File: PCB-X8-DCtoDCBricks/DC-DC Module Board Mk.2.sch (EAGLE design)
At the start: 151 parts, among them T1 FDN340P, T2 AP1117_LIN_REG, U3 LM1085IS-5.0

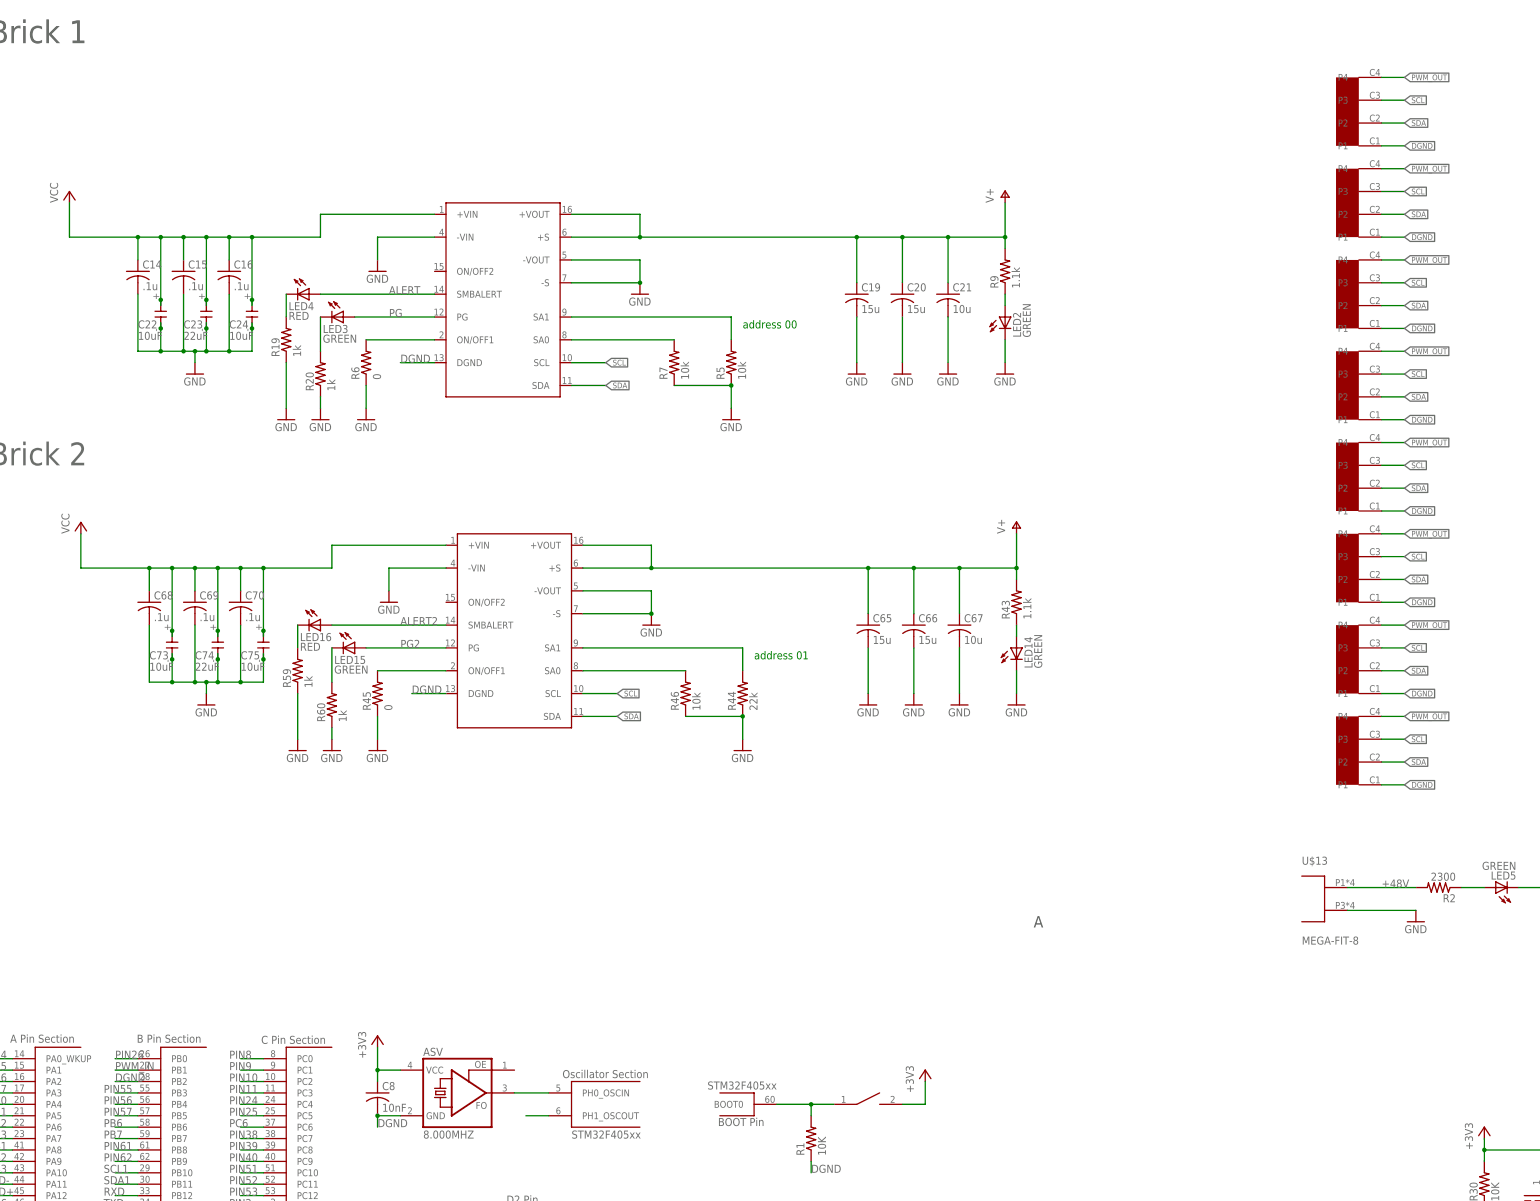
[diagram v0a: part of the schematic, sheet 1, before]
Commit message: top GND plane and clean up
Added top ground plane, cleaned up messy signals and other mistakes
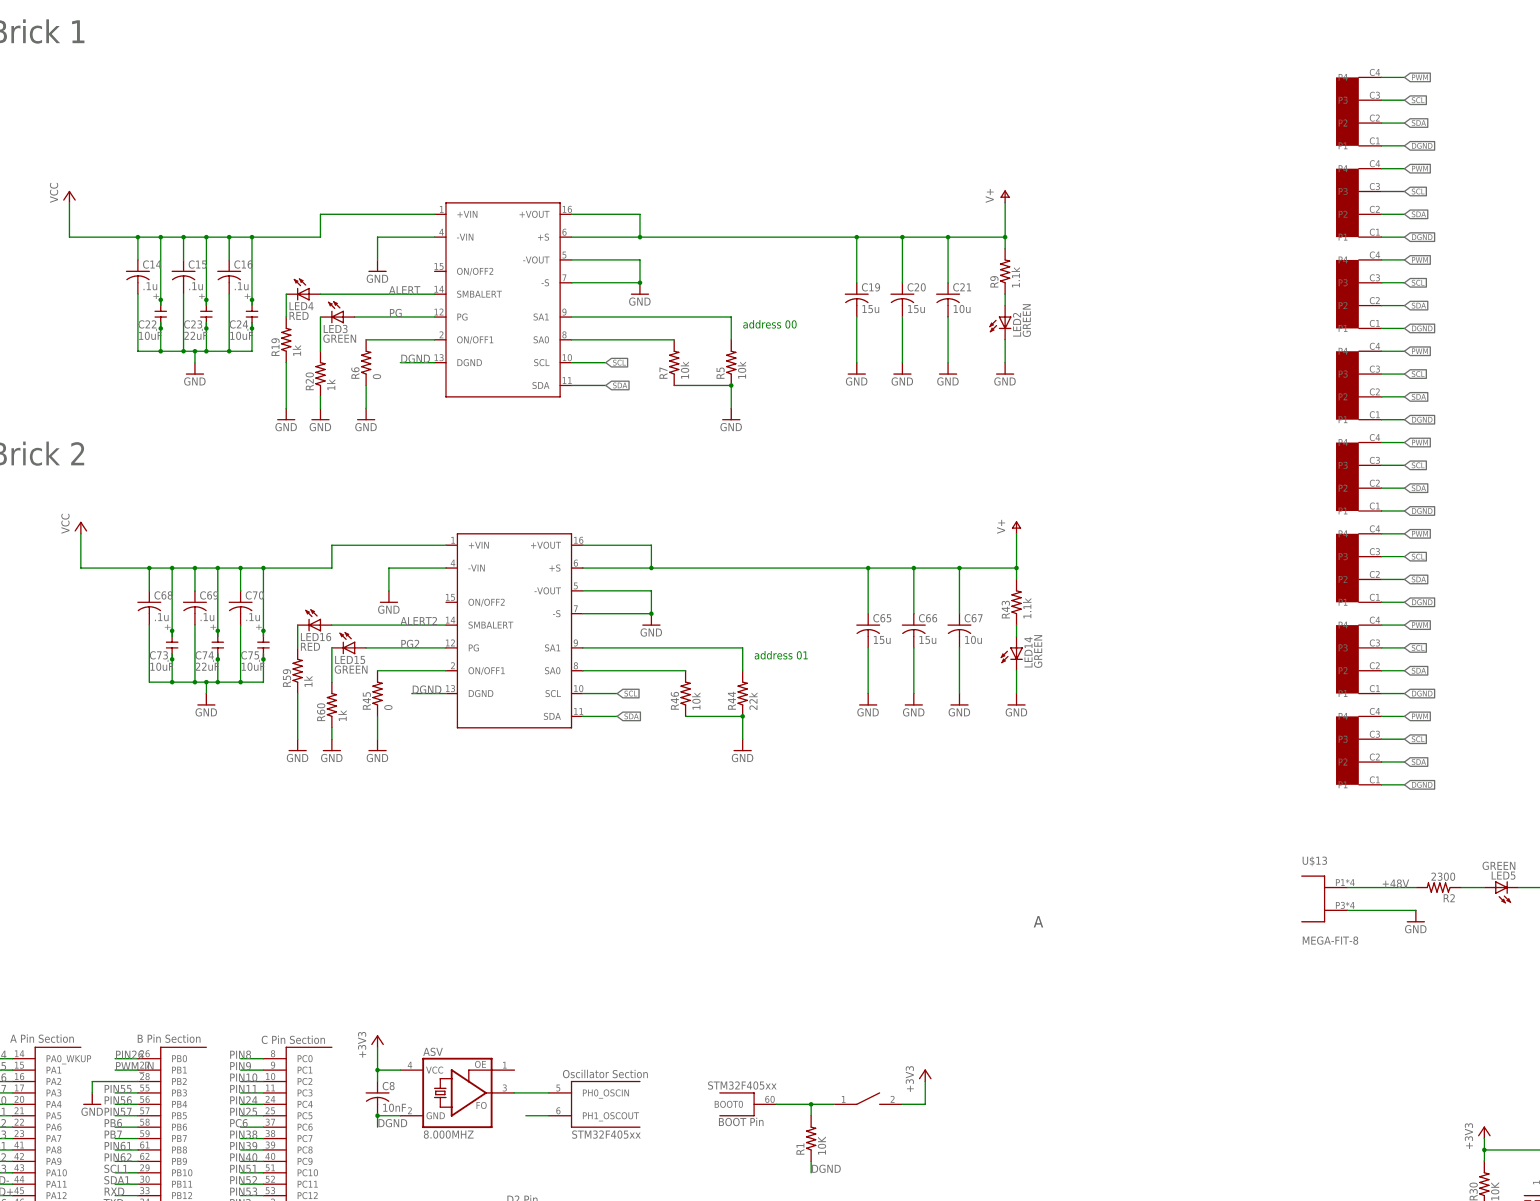
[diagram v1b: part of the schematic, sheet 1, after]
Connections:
- new net PWM: U$15.P4, U$20.P4, U$23.P4, U$24.P4, U$25.P4, U$26.P4, U$27.P4, U$28.P4
- net DGND: no longer U$5G$2.PB2
- net GND: now also U$5G$2.PB2
- net PWM_OUT: no longer U$15.P4, U$20.P4, U$23.P4, U$24.P4, U$25.P4, U$26.P4, U$27.P4, U$28.P4
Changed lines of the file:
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@@
 <?xml version="1.0" encoding="utf-8"?>
 <!DOCTYPE eagle SYSTEM "eagle.dtd">
-<eagle version="7.4.0">
+<eagle version="7.2.0">
 <drawing>
 <settings>
@@
 <part name="+3V3" library="supply1" deviceset="+3V3" device=""/>
 <part name="+3V4" library="supply1" deviceset="+3V3" device=""/>
+<part name="GND21" library="supply1" deviceset="GND" device=""/>
 <part name="FRAME3" library="frames" deviceset="FRAME_A_L" device=""/>
 <part name="D3" library="SparkFun-LED" deviceset="LED-YELLOW" device="0603" value="Yellow"/>
@@
 <instance part="+3V3" gate="G$1" x="193.04" y="-63.5"/>
 <instance part="+3V4" gate="G$1" x="99.06" y="-12.7"/>
+<instance part="GND21" gate="1" x="35.56" y="-27.94"/>
 <instance part="FRAME3" gate="G$1" x="292.1" y="-220.98"/>
 <instance part="FRAME3" gate="G$2" x="462.28" y="-220.98"/>
@@
 <wire x1="111.76" y1="165.1" x2="99.06" y2="165.1" width="0.1524" layer="91"/>
 <wire x1="99.06" y1="165.1" x2="99.06" y2="160.02" width="0.1524" layer="91"/>
+</segment>
+<segment>
+<pinref part="U$5" gate="G$2" pin="PB2"/>
+<wire x1="45.72" y1="-22.86" x2="35.56" y2="-22.86" width="0.1524" layer="91"/>
+<wire x1="35.56" y1="-22.86" x2="35.56" y2="-25.4" width="0.1524" layer="91"/>
+<pinref part="GND21" gate="1" pin="GND"/>
 </segment>
 <segment>
@@
 <label x="88.9" y="-213.36" size="1.778" layer="95"/>
 </segment>
-<segment>
-<pinref part="U$5" gate="G$2" pin="PB2"/>
-<wire x1="45.72" y1="-22.86" x2="40.64" y2="-22.86" width="0.1524" layer="91"/>
-<label x="40.64" y="-22.86" size="1.778" layer="95"/>
-</segment>
 </net>
 <net name="VCAP_1" class="0">
@@
 </segment>
 </net>
+<net name="PWM" class="0">
+<segment>
+<pinref part="U$15" gate="G$1" pin="P4"/>
+<wire x1="322.58" y1="200.66" x2="327.66" y2="200.66" width="0.1524" layer="91"/>
+<label x="327.66" y="200.66" size="1.27" layer="95" xref="yes"/>
+</segment>
+<segment>
+<pinref part="U$20" gate="G$1" pin="P4"/>
+<wire x1="322.58" y1="180.34" x2="327.66" y2="180.34" width="0.1524" layer="91"/>
+<label x="327.66" y="180.34" size="1.27" layer="95" xref="yes"/>
+</segment>
+<segment>
+<pinref part="U$23" gate="G$1" pin="P4"/>
+<wire x1="322.58" y1="160.02" x2="327.66" y2="160.02" width="0.1524" layer="91"/>
+<label x="327.66" y="160.02" size="1.27" layer="95" xref="yes"/>
+</segment>
+<segment>
+<pinref part="U$24" gate="G$1" pin="P4"/>
+<wire x1="322.58" y1="139.7" x2="327.66" y2="139.7" width="0.1524" layer="91"/>
+<label x="327.66" y="139.7" size="1.27" layer="95" xref="yes"/>
+</segment>
+<segment>
+<pinref part="U$25" gate="G$1" pin="P4"/>
+<wire x1="322.58" y1="119.38" x2="327.66" y2="119.38" width="0.1524" layer="91"/>
+<label x="327.66" y="119.38" size="1.27" layer="95" xref="yes"/>
+</segment>
+<segment>
+<pinref part="U$26" gate="G$1" pin="P4"/>
+<wire x1="322.58" y1="99.06" x2="327.66" y2="99.06" width="0.1524" layer="91"/>
+<label x="327.66" y="99.06" size="1.27" layer="95" xref="yes"/>
+</segment>
+<segment>
+<pinref part="U$27" gate="G$1" pin="P4"/>
+<wire x1="322.58" y1="78.74" x2="327.66" y2="78.74" width="0.1524" layer="91"/>
+<label x="327.66" y="78.74" size="1.27" layer="95" xref="yes"/>
+</segment>
+<segment>
+<pinref part="U$28" gate="G$1" pin="P4"/>
+<wire x1="322.58" y1="58.42" x2="327.66" y2="58.42" width="0.1524" layer="91"/>
+<label x="327.66" y="58.42" size="1.27" layer="95" xref="yes"/>
+</segment>
+</net>
 <net name="+12V4" class="0">
 <segment>
@@
 <label x="441.96" y="167.64" size="1.27" layer="95" xref="yes"/>
 </segment>
-<segment>
-<pinref part="U$28" gate="G$1" pin="P4"/>
-<wire x1="322.58" y1="58.42" x2="327.66" y2="58.42" width="0.1524" layer="91"/>
-<label x="327.66" y="58.42" size="1.27" layer="95" xref="yes"/>
-</segment>
-<segment>
-<pinref part="U$15" gate="G$1" pin="P4"/>
-<wire x1="322.58" y1="200.66" x2="327.66" y2="200.66" width="0.1524" layer="91"/>
-<label x="327.66" y="200.66" size="1.27" layer="95" xref="yes"/>
-</segment>
-<segment>
-<pinref part="U$20" gate="G$1" pin="P4"/>
-<wire x1="322.58" y1="180.34" x2="327.66" y2="180.34" width="0.1524" layer="91"/>
-<label x="327.66" y="180.34" size="1.27" layer="95" xref="yes"/>
-</segment>
-<segment>
-<pinref part="U$23" gate="G$1" pin="P4"/>
-<wire x1="322.58" y1="160.02" x2="327.66" y2="160.02" width="0.1524" layer="91"/>
-<label x="327.66" y="160.02" size="1.27" layer="95" xref="yes"/>
-</segment>
-<segment>
-<pinref part="U$24" gate="G$1" pin="P4"/>
-<wire x1="322.58" y1="139.7" x2="327.66" y2="139.7" width="0.1524" layer="91"/>
-<label x="327.66" y="139.7" size="1.27" layer="95" xref="yes"/>
-</segment>
-<segment>
-<pinref part="U$25" gate="G$1" pin="P4"/>
-<wire x1="322.58" y1="119.38" x2="327.66" y2="119.38" width="0.1524" layer="91"/>
-<label x="327.66" y="119.38" size="1.27" layer="95" xref="yes"/>
-</segment>
-<segment>
-<pinref part="U$26" gate="G$1" pin="P4"/>
-<wire x1="322.58" y1="99.06" x2="327.66" y2="99.06" width="0.1524" layer="91"/>
-<label x="327.66" y="99.06" size="1.27" layer="95" xref="yes"/>
-</segment>
-<segment>
-<pinref part="U$27" gate="G$1" pin="P4"/>
-<wire x1="322.58" y1="78.74" x2="327.66" y2="78.74" width="0.1524" layer="91"/>
-<label x="327.66" y="78.74" size="1.27" layer="95" xref="yes"/>
-</segment>
-</net>
+</net>
